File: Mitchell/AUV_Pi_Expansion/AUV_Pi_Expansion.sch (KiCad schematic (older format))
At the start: 63 parts, among them J1 40HAT, J2 CONN_02X02, J3 CONN_01X02, Q1 DMG2305UX, Q2 DMMT5401, U1 CAT24C32

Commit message: Updated Schematic and working bom .csv file
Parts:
- removed C1: 0.1u, Capacitor_SMD:C_0603_1608Metric, symbol Device:C_Small
- removed C2: 1u, Capacitor_SMD:C_0603_1608Metric, symbol Device:C_Small
- removed D5: USB, LED_SMD:LED_0603_1608Metric, symbol Device:LED_Small
- removed H5, H6, H7, H8: 3mm_Mounting_Hole, project_footprints:NPTH_3mm_ID, symbol Mechanical:MountingHole
- removed J2: CONN_02X02, Connector_PinHeader_2.54mm:PinHeader_2x02_P2.54mm_Vertical, symbol Connector_Generic:Conn_02x02_Odd_Even
- removed J3: CONN_01X02, Connector_PinHeader_2.54mm:PinHeader_1x02_P2.54mm_Vertical, symbol Connector_Generic:Conn_01x02
- removed Q1: DMG2305UX, Package_TO_SOT_SMD:SOT-23, symbol AUV_Pi_Expansion-rescue:DMG2305UX-raspberrypi_hat-pitest-rescue
- removed Q2: DMMT5401, Package_TO_SOT_SMD:SOT-23-6, symbol AUV_Pi_Expansion-rescue:DMMT5401-raspberrypi_hat-pitest-rescue
- removed R10, R11, R12: DNP, Resistor_SMD:R_0603_1608Metric_Pad0.84x1.00mm_HandSolder, symbol Device:R
- removed R13, R8: 10K, Resistor_SMD:R_0603_1608Metric_Pad0.84x1.00mm_HandSolder, symbol Device:R
- removed R14, R15: 3.9K, Resistor_SMD:R_0603_1608Metric_Pad0.84x1.00mm_HandSolder, symbol Device:R
- removed R7: 1k, Resistor_SMD:R_0603_1608Metric, symbol Device:R_Small_US
- removed R9: 47K, Resistor_SMD:R_0603_1608Metric_Pad0.84x1.00mm_HandSolder, symbol Device:R
- removed RN1: 10k, Resistor_SMD:R_Array_Convex_4x0603, symbol Device:R_Pack04
- removed TP4: USB, TestPoint:TestPoint_Pad_D1.0mm, symbol Connector:TestPoint
- removed TP8: GND, TestPoint:TestPoint_Pad_D1.0mm, symbol Connector:TestPoint
- removed U1: CAT24C32, Package_SOIC:SOIC-8_3.9x4.9mm_P1.27mm, symbol AUV_Pi_Expansion-rescue:CAT24C32-raspberrypi_hat-pitest-rescue
- added J10: ESC3C, Connector_JST:JST_SH_SM02B-SRSS-TB_1x02-1MP_P1.00mm_Horizontal, symbol Connector_Generic:Conn_01x02
- added J11: ESC2C, Connector_JST:JST_SH_SM02B-SRSS-TB_1x02-1MP_P1.00mm_Horizontal, symbol Connector_Generic:Conn_01x02
- added J12: ESC1C, Connector_JST:JST_SH_SM02B-SRSS-TB_1x02-1MP_P1.00mm_Horizontal, symbol Connector_Generic:Conn_01x02
- added J14: ESC6P, µ104KiCAD_connectors:XT30PW-M, symbol Connector_Generic:Conn_01x02
- added J15: ESC5P, µ104KiCAD_connectors:XT30PW-M, symbol Connector_Generic:Conn_01x02
- added J17: ESC4P, µ104KiCAD_connectors:XT30PW-M, symbol Connector_Generic:Conn_01x02
- added J18: ESC6C, Connector_JST:JST_SH_SM02B-SRSS-TB_1x02-1MP_P1.00mm_Horizontal, symbol Connector_Generic:Conn_01x02
- added J19: ESC5C, Connector_JST:JST_SH_SM02B-SRSS-TB_1x02-1MP_P1.00mm_Horizontal, symbol Connector_Generic:Conn_01x02
- added J2: FAN, Connector_PinHeader_2.54mm:PinHeader_1x02_P2.54mm_Vertical, symbol Connector_Generic:Conn_01x02
- added J20: ESC4C, Connector_JST:JST_SH_SM02B-SRSS-TB_1x02-1MP_P1.00mm_Horizontal, symbol Connector_Generic:Conn_01x02
- added J6: ESC3P, µ104KiCAD_connectors:XT30PW-M, symbol Connector_Generic:Conn_01x02
- added J7: ESC2P, µ104KiCAD_connectors:XT30PW-M, symbol Connector_Generic:Conn_01x02
- added J8: ESC1P, µ104KiCAD_connectors:XT30PW-M, symbol Connector_Generic:Conn_01x02
- added Logo18: Cod, silk:cod, symbol u104_KICAD_misc:LogoBlock
- D1: Desc Blue -> Green - Vf sub 3V for <10mA; LCSC C72041 -> C72043
- J1: LCSC (none) -> C725892
- R1: value 4.7k -> 3.9k; Desc 4.7KΩ (4701) ±1% -> (none); LCSC C23162 -> C118399
- R2: value 10k -> 3.9k; Desc 10KΩ (1002) ±1% -> (none); LCSC C25804 -> C118399
- R3: value 100k -> 100; Desc 100KΩ (1003) ±1% -> 100; LCSC C25803 -> C22775
- R4: value 1M -> 100; Desc 1MΩ (1004) ±1% -> 100; LCSC C22935 -> C22775
- R5: value 0 -> 1k; Desc 0Ω (0R0) ±1% -> 1KΩ (1001) ±1%; LCSC C21189 -> C21190
- R6: value 33 -> 4.7k; Desc 33Ω (33R0) ±1% -> 4.7KΩ (4701) ±1%; LCSC C23140 -> C23162
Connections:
- net +3V3: now also R1.1, R2.1, R4.1
- net +5V: now also R5.1
- net +V: now also R6.1, J14.2 (Pin_2), J15.2 (Pin_2), J17.2 (Pin_2), J6.2 (Pin_2), J7.2 (Pin_2), J8.2 (Pin_2)
- net GND: now also R3.2, J14.1 (Pin_1), J15.1 (Pin_1), J17.1 (Pin_1), J2.1 (Pin_1), J6.1 (Pin_1), J7.1 (Pin_1), J8.1 (Pin_1)
- net P3V3_HAT: now also J1.17 (P3V3)
- net RXD\GPIO15: now reaches J1.10 (BCM15)
- net LOAD0: now reaches J1.11 (BCM17)
- net LED_USR2: now reaches J1.12 (BCM18)
- net LOAD1: now reaches J1.13 (BCM27)
- net LEAK_2: now reaches J1.15 (BCM22)
- net BNO_INT: now reaches J1.16 (BCM23)
- net BNO_BL_IND: now reaches J1.18 (BCM24)
- net MOSI0\GPIO10: now reaches J1.19 (BCM10)
- net MISO0\GPIO9: now reaches J1.21 (BCM9)
- net BNO_~RST: now reaches J1.22 (BCM25)
- net SCLK0\GPIO11: now reaches J1.23 (BCM11)
- net ~CE0~\GPIO8: now reaches J1.24 (BCM8)
- net ~CE1~\GPIO7: now reaches J1.26 (BCM7)
- net GCLK1\GPIO5: now reaches J1.29 (BCM5)
- net SDA\GPIO2: now reaches J1.3 (BCM2)
- net SDA\GPIO2: now also R1.2
- net GCLK2\GPIO6: now reaches J1.31 (BCM6)
- net G_DRV_LED: now reaches J1.32 (BCM12)
- net PWM1\GPIO12: now reaches J1.33 (BCM13)
- net MISO1\GPIO19: now reaches J1.35 (BCM19)
- net EXT_TEMP: now reaches J1.36 (BCM16)
- net LEAK_1: now reaches J1.37 (BCM26)
- net MOSI1\GPIO20: now reaches J1.38 (BCM20)
- net SCLK1\GPIO21: now reaches J1.40 (BCM21)
- net SCL\GPIO3: now reaches J1.5 (BCM3)
- net SCL\GPIO3: now also R2.2
- net LED_USR1: now reaches J1.7 (BCM4)
- net LED_USR1: now also D1.2 (A)
- net TXD\GPIO14: now reaches J1.8 (BCM14)
- net at R5.2: now also D3.2 (A)
- net at D2.2 (A): now also R4.2
- net at D4.2 (A): now also R6.2
- net at R3.1: now also D1.1 (K)
- net ID_SD_EEPROM renamed ID_SD_EEPROM\GPIO0
- new net 5V_EXT\POE: J2.2 (Pin_2)
- new net CANH: J10.2 (Pin_2), J11.2 (Pin_2), J12.2 (Pin_2), J18.2 (Pin_2), J19.2 (Pin_2), J20.2 (Pin_2)
- new net CANL: J10.1 (Pin_1), J11.1 (Pin_1), J12.1 (Pin_1), J18.1 (Pin_1), J19.1 (Pin_1), J20.1 (Pin_1)
- no-connect marks 6 -> 14
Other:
- note added: "1) Assemble 5V pwr supply first and trim pot to 5V"
- note added: "1) See Descriptions for fuses, connector housings\n2) Find Waterproof temp sensor from bin\n3) Append .csv to %O in output command for gen."
- note added: "40-Pin HAT Connectors\n"
- note added: "ESC\n"
- note added: "EXTRA BOM:\n- Fuses\nHardware\n- C79822 : M3 Standoffs w/ threaded insert\n- C24867 : M3 Washers\n- C24866 : M3 Nuts\n- C357547 : M3 Long Screws\n- C357542 : M3 Short Screws\n"
- note added: "FAN\n"
- note added: "GCLK0\GPIO4"
- note added: "GCLK1\GPIO5"
- note added: "GCLK2\GPIO6"
- note added: "GPIO16"
- note added: "GPIO17"
- note added: "GPIO22"
- note added: "GPIO23"
- note added: "GPIO24"
- note added: "GPIO25"
- note added: "GPIO26"
- note added: "GPIO27"
- note added: "Interface\n"
- note added: "MISO0\GPIO9"
- note added: "MOSI0\GPIO10"
- note added: "POE\n"
- note added: "PWM0\GPIO12"
- note added: "PWM0\GPIO18"
- note added: "Power"
- note added: "SCLK0\GPIO11"
- note added: "Sensors\n"
- note added: "~CE0~\GPIO8"
- note removed: "40-Pin HAT Connector"
- note removed: "5V Powered HAT Protection"
- note removed: "EEPROM WRITE ENABLE"
- note removed: "EXTRA BOM:\n- X\nHardware\n- C79822 : M3 Standoffs w/ threaded insert\n- C24867 : M3 Washers\n- C24866 : M3 Nuts\n- C357547 : M3 Long Screws\n- C357542 : M3 Short Screws\n"
- note removed: "FLEXIBLE POWER SELECTION"
- note removed: "HAT EEPROM"
- note removed: "HAT spec indicates to NEVER\npower the 3.3V pins on the Raspberry Pi \nfrom the HAT header. Only connect the 3.3V\npower from the Pi if the HAT does not have\n3.3V on board.\n\nIF you are designing a board that could\neither be powered by the Pi or from the HAT\nthe jumpers here can be used.\n\nIn most cases, either design the HAT \nto provide the 5V to the Pi and use the\nprotection circuit abov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"
- note removed: "Mounting Holes"
- note removed: "Part Bank:"
- note removed: "Pullup Resistors"
- note removed: "Subsection Label\n"
- note removed: "The HAT spec requires this EEPROM with system information\nto be in place in order to be called a HAT. It should be set up as write\nprotected (WP pin held high), so it may be desirable to either put a \njumper as shown to enable writing, or to hook up a spare IO pin to do so."
- note removed: "These are just pullup resistors for the I2C bus on the EEPROM.\nThe resistor values are per the HAT spec."
- note removed: "This is based on the official Raspberry Pi spec to be able to call an extension board a HAT.\nhttps://github.com/raspberrypi/hats/blob/master/designguide.md"
- note removed: "This is the recommended 5V rail protection for \na HAT with power going to the Pi.\nSee https://github.com/raspberrypi/hats/blob/master/designguide.md#back-powering-the-pi-via-the-j8-gpio-header"
- moved on the sheet: D2, D3, D4, J1, JP1, TP1, TP2, TP3, TP5, TP6, TP7

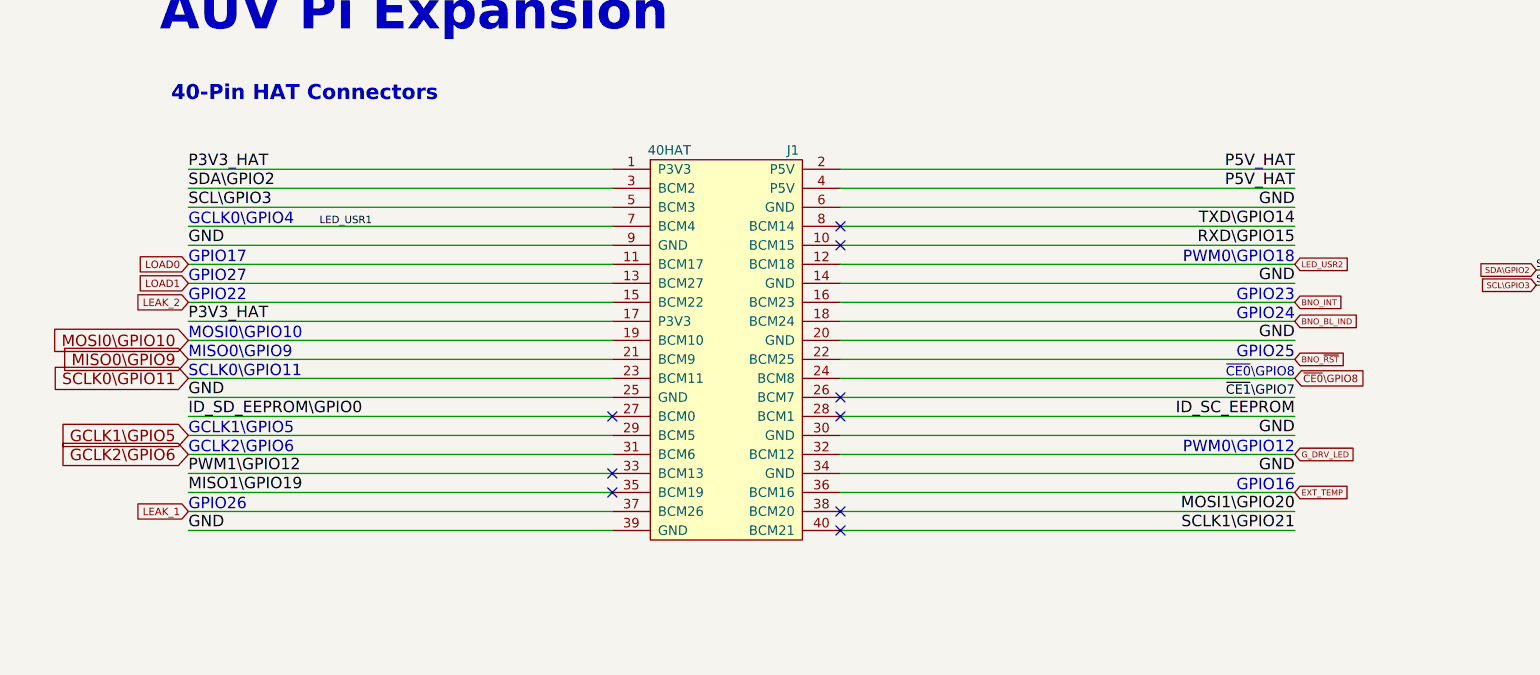
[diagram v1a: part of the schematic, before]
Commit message: Sch label net changes to global tags
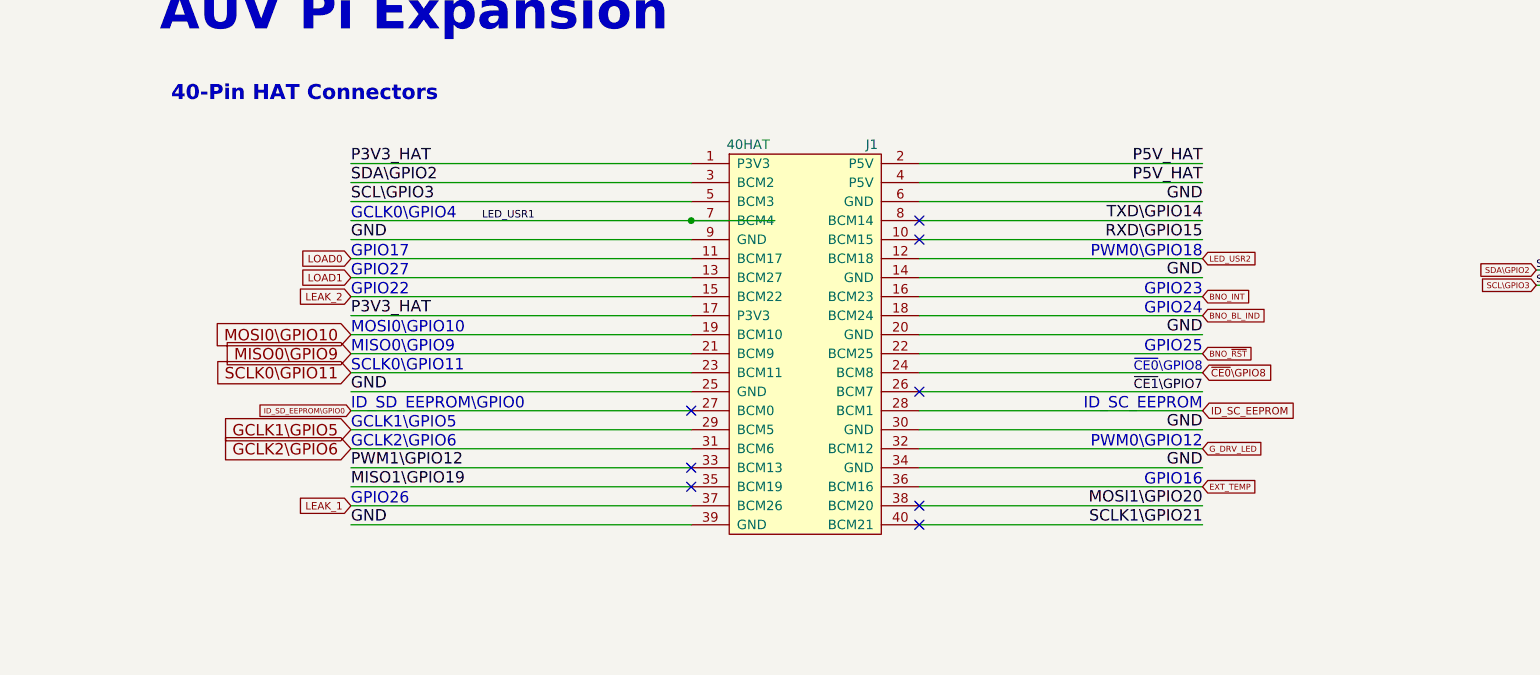
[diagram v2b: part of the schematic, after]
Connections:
- no-connect marks 14 -> 13
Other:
- note added: "ID_SC_EEPROM"
- note added: "ID_SD_EEPROM\GPIO0"
- moved on the sheet: J1
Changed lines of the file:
@@
 L AUV_Pi_Expansion-rescue:OX40HAT-raspberrypi_hat-pitest-rescue J1
 U 1 1 58DFC771
-P 3560 1660
-F 0 "J1" H 3910 1760 50  0000 C CNN
-F 1 "40HAT" H 3260 1760 50  0000 C CNN
-F 2 "Connector_PinSocket_2.54mm:PinSocket_2x20_P2.54mm_Vertical" H 3560 1860 50  0001 C CNN
-F 3 "https://www.raspberrypi.org/documentation/hardware/raspberrypi/schematics/rpi_SCH_3bplus_1p0_reduced.pdf" H 2860 1660 50  0001 C CNN
-F 4 "C725892" H 3560 1660 50  0001 C CNN "LCSC"
-F 5 "" H 3560 1660 50  0001 C CNN "Digi"
-F 6 "" H 3560 1660 50  0001 C CNN "Desc"
-	1    3560 1660
+P 3975 1630
+F 0 "J1" H 4325 1730 50  0000 C CNN
+F 1 "40HAT" H 3675 1730 50  0000 C CNN
+F 2 "Connector_PinSocket_2.54mm:PinSocket_2x20_P2.54mm_Vertical" H 3975 1830 50  0001 C CNN
+F 3 "https://www.raspberrypi.org/documentation/hardware/raspberrypi/schematics/rpi_SCH_3bplus_1p0_reduced.pdf" H 3275 1630 50  0001 C CNN
+F 4 "C725892" H 3975 1630 50  0001 C CNN "LCSC"
+F 5 "" H 3975 1630 50  0001 C CNN "Digi"
+F 6 "" H 3975 1630 50  0001 C CNN "Desc"
+	1    3975 1630
 	1    0    0    -1
 $EndComp
-Text Label 730  3560 0    60   ~ 0
+Text Label 1585 3530 0    60   ~ 0
 GND
 Wire Wire Line
-	2960 3560 730  3560
-Text Label 730  2960 0    60   ~ 0
-ID_SD_EEPROM\GPIO0
+	3375 3530 1585 3530
 Wire Wire Line
-	2960 2960 730  2960
-Text Label 730  2860 0    60   ~ 0
+	3375 2930 1585 2930
+Text Label 1585 2830 0    60   ~ 0
 GND
 Wire Wire Line
-	2960 2860 730  2860
+	3375 2830 1585 2830
 Wire Wire Line
-	2960 2060 730  2060
+	3375 2030 1585 2030
 Wire Wire Line
-	2960 1660 730  1660
+	3375 1630 1585 1630
 Wire Wire Line
-	4160 2260 6550 2260
+	4575 2230 6065 2230
 Wire Wire Line
-	4160 2560 6550 2560
+	4575 2530 6065 2530
 Wire Wire Line
-	4160 2960 6550 2960
+	4575 2930 6065 2930
 Wire Wire Line
-	4160 3060 6550 3060
+	4575 3030 6065 3030
 Wire Wire Line
-	4160 3260 6550 3260
-Text Label 6550 2260 2    60   ~ 0
+	4575 3230 6065 3230
+Text Label 6065 2230 2    60   ~ 0
 GND
-Text Label 6550 2560 2    60   ~ 0
+Text Label 6065 2530 2    60   ~ 0
 GND
-Text Label 6550 3060 2    60   ~ 0
+Text Label 6065 3030 2    60   ~ 0
 GND
-Text Label 6550 2960 2    60   ~ 0
-ID_SC_EEPROM
-Text Label 6550 3260 2    60   ~ 0
+Text Label 6065 3230 2    60   ~ 0
 GND
-Text Label 6550 1860 2    60   ~ 0
+Text Label 6065 1830 2    60   ~ 0
 GND
-Text Label 6550 1760 2    60   ~ 0
+Text Label 6065 1730 2    60   ~ 0
 P5V_HAT
-Text Label 6550 1660 2    60   ~ 0
+Text Label 6065 1630 2    60   ~ 0
 P5V_HAT
 $Comp
@@
 $EndComp
 Wire Wire Line
-	4160 1660 6550 1660
+	4575 1630 6065 1630
 Wire Wire Line
-	4160 1760 6550 1760
+	4575 1730 6065 1730
 Wire Wire Line
-	4160 1860 6550 1860
+	4575 1830 6065 1830
 Wire Wire Line
-	730  1960 2960 1960
+	1585 1930 3375 1930
 Wire Wire Line
-	730  2160 2960 2160
+	1585 2130 3375 2130
 Wire Wire Line
-	730  2260 2960 2260
+	1585 2230 3375 2230
 Wire Wire Line
-	730  2360 2960 2360
+	1585 2330 3375 2330
 Wire Wire Line
-	730  2460 2960 2460
+	1585 2430 3375 2430
 Wire Wire Line
-	730  2560 2960 2560
+	1585 2530 3375 2530
 Wire Wire Line
-	730  2660 2960 2660
+	1585 2630 3375 2630
 Wire Wire Line
-	730  3060 2960 3060
+	1585 3030 3375 3030
 Wire Wire Line
-	730  3160 2960 3160
+	1585 3130 3375 3130
 Wire Wire Line
-	730  3260 2960 3260
+	1585 3230 3375 3230
 Wire Wire Line
-	730  3360 2960 3360
+	1585 3330 3375 3330
 Wire Wire Line
-	730  2760 2960 2760
+	1585 2730 3375 2730
 Wire Wire Line
-	730  3460 2960 3460
+	1585 3430 3375 3430
 Wire Wire Line
-	4160 2660 6550 2660
+	4575 2630 6065 2630
 Wire Wire Line
-	4160 2760 6550 2760
+	4575 2730 6065 2730
 Wire Wire Line
-	4160 2860 6550 2860
+	4575 2830 6065 2830
 Wire Wire Line
-	4160 1960 6550 1960
+	4575 1930 6065 1930
 Wire Wire Line
-	4160 2060 6550 2060
+	4575 2030 6065 2030
 Wire Wire Line
-	4160 2160 6550 2160
+	4575 2130 6065 2130
 Wire Wire Line
-	4160 3360 6550 3360
+	4575 3330 6065 3330
 Wire Wire Line
-	4160 3460 6550 3460
+	4575 3430 6065 3430
 Wire Wire Line
-	4160 3560 6550 3560
+	4575 3530 6065 3530
 Wire Wire Line
-	4160 2360 6550 2360
+	4575 2330 6065 2330
 Wire Wire Line
-	4160 2460 6550 2460
+	4575 2430 6065 2430
 Wire Wire Line
-	4160 3160 6550 3160
-Text Label 730  2460 0    60   ~ 0
+	4575 3130 6065 3130
+Text Label 1585 2430 0    60   ~ 0
 P3V3_HAT
-Text Label 730  3260 0    60   ~ 0
+Text Label 1585 3230 0    60   ~ 0
 PWM1\GPIO12
-Text Label 730  3360 0    60   ~ 0
+Text Label 1585 3330 0    60   ~ 0
 MISO1\GPIO19
-Text Label 6550 1960 2    60   ~ 0
+Text Label 6065 1930 2    60   ~ 0
 TXD\GPIO14
-Text Label 6550 2060 2    60   ~ 0
+Text Label 6065 2030 2    60   ~ 0
 RXD\GPIO15
-Text Label 6550 2860 2    49   ~ 0
+Text Label 6065 2830 2    49   ~ 0
 ~CE1~\GPIO7
-Text Label 6550 3460 2    60   ~ 0
+Text Label 6065 3430 2    60   ~ 0
 MOSI1\GPIO20
-Text Label 6550 3560 2    60   ~ 0
+Text Label 6065 3530 2    60   ~ 0
 SCLK1\GPIO21
 Text Notes 9090 2170 0    79   ~ 16
@@
 Wire Wire Line
 	8250 2810 8250 2870
-Text Label 1420 1960 0    39   ~ 0
+Text Label 2275 1930 0    39   ~ 0
 LED_USR1
 $Comp
@@
 FAN\n
 Wire Wire Line
-	730  1860 2960 1860
+	1585 1830 3375 1830
 Wire Wire Line
-	730  1760 2960 1760
-Text Label 730  2060 0    60   ~ 0
+	1585 1730 3375 1730
+Text Label 1585 2030 0    60   ~ 0
 GND
-Text Label 730  1860 0    60   ~ 0
+Text Label 1585 1830 0    60   ~ 0
 SCL\GPIO3
-Text Label 730  1760 0    60   ~ 0
+Text Label 1585 1730 0    60   ~ 0
 SDA\GPIO2
-Text Label 730  1660 0    60   ~ 0
+Text Label 1585 1630 0    60   ~ 0
 P3V3_HAT
 Text Label 7820 2190 0    39   ~ 0
@@
 Wire Wire Line
 	7820 2190 8170 2190
-Text Notes 6550 2160 2    60   ~ 0
+Text Notes 6065 2130 2    60   ~ 0
 PWM0\GPIO18
-Text Notes 730  1960 0    60   ~ 0
+Text Notes 1585 1930 0    60   ~ 0
 GCLK0\GPIO4
-Text Notes 730  2160 0    60   ~ 0
+Text Notes 1585 2130 0    60   ~ 0
 GPIO17
-Text Notes 730  2260 0    60   ~ 0
+Text Notes 1585 2230 0    60   ~ 0
 GPIO27
-Text Notes 730  2360 0    60   ~ 0
+Text Notes 1585 2330 0    60   ~ 0
 GPIO22
-Text Notes 6550 2360 2    60   ~ 0
+Text Notes 6065 2330 2    60   ~ 0
 GPIO23
-Text Notes 6550 2460 2    60   ~ 0
+Text Notes 6065 2430 2    60   ~ 0
 GPIO24
-Text Notes 730  3460 0    60   ~ 0
+Text Notes 1585 3430 0    60   ~ 0
 GPIO26
-Text Notes 6550 3360 2    60   ~ 0
+Text Notes 6065 3330 2    60   ~ 0
 GPIO16
-Text Notes 6550 2660 2    60   ~ 0
+Text Notes 6065 2630 2    60   ~ 0
 GPIO25
-Text Notes 6550 3160 2    60   ~ 0
+Text Notes 6065 3130 2    60   ~ 0
 PWM0\GPIO12
-NoConn ~ 2960 2960
-NoConn ~ 2960 3260
-NoConn ~ 2960 3360
-NoConn ~ 4160 3560
-NoConn ~ 4160 3460
-NoConn ~ 4160 2960
-NoConn ~ 4160 2860
-NoConn ~ 4160 2060
-NoConn ~ 4160 1960
-Text GLabel 6550 2460 2    31   Input ~ 0
+NoConn ~ 3375 2930
+NoConn ~ 3375 3230
+NoConn ~ 3375 3330
+NoConn ~ 4575 3530
+NoConn ~ 4575 3430
+NoConn ~ 4575 2830
+NoConn ~ 4575 2030
+NoConn ~ 4575 1930
+Text GLabel 6065 2430 2    31   Input ~ 0
 BNO_BL_IND
-Text GLabel 6550 2360 2    31   Input ~ 0
+Text GLabel 6065 2330 2    31   Input ~ 0
 BNO_INT
-Text GLabel 6550 2160 2    31   Input ~ 0
+Text GLabel 6065 2130 2    31   Input ~ 0
 LED_USR2
-Text GLabel 6550 3360 2    31   Input ~ 0
+Text GLabel 6065 3330 2    31   Input ~ 0
 EXT_TEMP
 Text GLabel 7820 2270 0    31   Input ~ 0
@@
 Text GLabel 7820 2190 0    31   Input ~ 0
 SDA\GPIO2
-Text GLabel 6550 3160 2    31   Input ~ 0
+Text GLabel 6065 3130 2    31   Input ~ 0
 G_DRV_LED
-Text GLabel 6550 2660 2    31   Input ~ 0
+Text GLabel 6065 2630 2    31   Input ~ 0
 BNO_~RST
-Text GLabel 730  3460 0    39   Input ~ 0
+Text GLabel 1585 3430 0    39   Input ~ 0
 LEAK_1
-Text GLabel 730  2360 0    39   Input ~ 0
+Text GLabel 1585 2330 0    39   Input ~ 0
 LEAK_2
-Text GLabel 730  2260 0    39   Input ~ 0
+Text GLabel 1585 2230 0    39   Input ~ 0
 LOAD1
-Text GLabel 730  2160 0    39   Input ~ 0
+Text GLabel 1585 2130 0    39   Input ~ 0
 LOAD0
-Text GLabel 730  2560 0    60   Input ~ 0
+Text GLabel 1585 2530 0    60   Input ~ 0
 MOSI0\GPIO10
-Text GLabel 730  2660 0    60   Input ~ 0
+Text GLabel 1585 2630 0    60   Input ~ 0
 MISO0\GPIO9
-Text GLabel 6550 2760 2    39   Input ~ 0
+Text GLabel 6065 2730 2    39   Input ~ 0
 ~CE0~\GPIO8
-Text GLabel 730  2760 0    60   Input ~ 0
+Text GLabel 1585 2730 0    60   Input ~ 0
 SCLK0\GPIO11
-Text Notes 6550 2760 2    49   ~ 0
+Text Notes 6065 2730 2    49   ~ 0
 ~CE0~\GPIO8
-Text Notes 730  2560 0    60   ~ 0
+Text Notes 1585 2530 0    60   ~ 0
 MOSI0\GPIO10
-Text Notes 730  2660 0    60   ~ 0
+Text Notes 1585 2630 0    60   ~ 0
 MISO0\GPIO9
-Text Notes 730  2760 0    60   ~ 0
+Text Notes 1585 2730 0    60   ~ 0
 SCLK0\GPIO11
-Text GLabel 730  3060 0    60   Input ~ 0
+Text GLabel 1585 3030 0    60   Input ~ 0
 GCLK1\GPIO5
-Text Notes 730  3060 0    60   ~ 0
+Text Notes 1585 3030 0    60   ~ 0
 GCLK1\GPIO5
-Text GLabel 730  3160 0    60   Input ~ 0
+Text GLabel 1585 3130 0    60   Input ~ 0
 GCLK2\GPIO6
-Text Notes 730  3160 0    60   ~ 0
+Text Notes 1585 3130 0    60   ~ 0
 GCLK2\GPIO6
+Connection ~ 3375 1930
+Wire Wire Line
+	3375 1930 3815 1930
+Text GLabel 6065 2930 2    39   Input ~ 0
+ID_SC_EEPROM
+Text GLabel 1585 2930 0    28   Input ~ 0
+ID_SD_EEPROM\GPIO0
+Text Notes 6065 2930 2    60   ~ 0
+ID_SC_EEPROM
+Text Notes 1585 2930 0    60   ~ 0
+ID_SD_EEPROM\GPIO0
 $EndSCHEMATC

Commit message: Pi4 Remake Done
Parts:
- removed Logo12: Trident, silk:trident, symbol u104_KICAD_misc:LogoBlock
- removed Logo13: Starfish, silk:starfish, symbol u104_KICAD_misc:LogoBlock
- removed Logo15: Dhelmet, silk:diverhel, symbol u104_KICAD_misc:LogoBlock
- removed Logo17: Anchor, silk:anchor, symbol u104_KICAD_misc:LogoBlock
- removed Logo2: luckyvolt1, silk:luckyvolt_small_10mm, symbol u104_KICAD_misc:LogoBlock
- removed Logo3: luckyvolt2, silk:luckyvolt_small_15mm, symbol u104_KICAD_misc:LogoBlock
- removed Logo4: luckyvolt3, silk:luckyvolt_small_20mm, symbol u104_KICAD_misc:LogoBlock
- removed Logo5: luckyvolt4, silk:luckyvolt_small_31mm, symbol u104_KICAD_misc:LogoBlock
- J1: Desc (none) -> Digi 1528-2235-ND for cable
- J10, J11, J12, J18, J19, J20: footprint Connector_JST:JST_SH_SM02B-SRSS-TB_1x02-1MP_P1.00mm_Horizontal -> Connector_JST:JST_SH_BM02B-SRSS-TB_1x02-1MP_P1.00mm_Vertical; Desc JST SR/SZ - SH compatible -> JST SR/SZ - SH compatible Vertical; LCSC C160402 -> C160388
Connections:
- net GND: now also D1.1 (K); no longer R3.2
- net LED_USR1: now also R3.1; no longer D1.2 (A)
- net P3V3_HAT: no longer J1.17 (P3V3)
- new net: D1.2 (A), R3.2
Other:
- note added: ""POE"\n"
- note added: "*GCLK2\GPIO6 INT for CAN, not important\n"
- note added: "P3V3_HAT"
- note added: "PWM1\GPIO12"
- note removed: "POE\n"
- moved on the sheet: D1, R3
